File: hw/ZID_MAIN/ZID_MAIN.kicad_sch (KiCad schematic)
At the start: 201 parts, among them J1 Conn 1x04 0.1" Socket, J10 FFC/FPC-40 Socket, J11 JST-PH-K B6B, J12 JST-PH-K B6B, J13 Conn_02x05_PINHDR_2.54mm, J14 USB-C PWR ONLY, J2 JST-PH-K B6B, J3 Conn 1x02 0.1" pin, J4 Conn 1x03 0.1" pin, J5 Conn 1x08 0.1" pin, J6 Conn 1x08 0.1" pin, J7 Conn 2x04 0.1" pin, J8 Conn 2x02 0.1" pin, J9 Conn 2x04 0.1" pin, M1 WS-RP2040-Zero, SW1 SW_Push, SW2 SW_DIP_x02, U1 OSC-20MHz, U10 27WZ06, U11 74LVC125AS, U12 74LVC273, U13 74FCT2245, U14 AS7C1024B, U16 74FCT2245, U18 ATF1508AS, U2 74FCT2245, U20 74FCT2244, U22 ATF1504AS-44T, U23 74AHCT00, U24 74FCT2244, U25 ATF1504AS-44T, U26 ATF1504AS-44T, U27 ATF1504AS-44T, U28 ATF1504AS-44T, U3 24LC32, U4 MIC2775, U5 SST39SF010, U6 74LVC245, U7 74FCT2245, U8 74AHCT14, U9 Z80 C20MHz-PLCC

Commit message: SCHM: Updates per SM. PLD: comment corrections. PCB: start routing.
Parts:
- removed C12, C13, C14, C15, C16, C17, C18, C19, C35, C36, C37, C38: 0.1uF, Capacitor_SMD:C_0603_1608Metric, symbol Device:C_Small
- removed JC1, JD1: SolderJumper_2_Open, Jumper:SolderJumper-2_P1.3mm_Open_TrianglePad1.0x1.5mm, symbol Jumper:SolderJumper_2_Open
- removed JP5: Jumper_2_Small_Bridged, Connector_PinHeader_2.00mm:PinHeader_1x02_P2.00mm_Vertical, symbol Jumper:Jumper_2_Small_Bridged
- removed OP4: AES-Option_A-B_2mm, Connector_PinHeader_2.00mm:PinHeader_1x03_P2.00mm_Vertical, symbol AES_Library:AES-Option_A-B_2mm
- removed R43: 4.7k, Resistor_SMD:R_0805_2012Metric, symbol Device:R_Small_US
- removed SPRU8F1: Conn_01x03_Pin, Connector_PinHeader_2.00mm:PinHeader_1x03_P2.00mm_Vertical, symbol Connector:Conn_01x03_Pin
- removed TP12, TP26, TP28, TP29, TP31, TP32, TP33, TP34: TestPoint, TestPoint:TestPoint_THTPad_D1.0mm_Drill0.5mm, symbol Connector:TestPoint
- removed U25, U26, U27, U28: ATF1504AS-44T, Package_QFP:TQFP-44_10x10mm_P0.8mm, symbol AES_Library:ATF1504AS-44T-AES
- added DBOPT1: AES-Option_A-B_2mm, Connector_PinHeader_2.00mm:PinHeader_1x03_P2.00mm_Vertical, symbol AES_Library:AES-Option_A-B_2mm
- added J15: Conn 2x03 pin hdr 0.1", Connector_PinHeader_2.00mm:PinHeader_2x03_P2.00mm_Vertical, symbol Connector_Generic:Conn_02x03_Odd_Even
- added R34: 100k, Resistor_SMD:R_0805_2012Metric, symbol Device:R_Small_US
- added TP19, TP20, TP23, TP24: TestPoint, TestPoint:TestPoint_THTPad_D1.0mm_Drill0.5mm, symbol Connector:TestPoint
- added U15: ATF1508AS, Package_QFP:TQFP-100_14x14mm_P0.5mm, symbol AES_Library:ATF1508AS-AES
- R14: value 10k -> 100K; footprint Resistor_SMD:R_0805_2012Metric -> Resistor_SMD:R_0805_2012Metric_Pad1.20x1.40mm_HandSolder
- R23: value 10k -> 100k
- R42: value 4.7k -> 100k
- RN1, RN2: value 20k -> 100k
- TP17, TP18, TP21, TP22: Function IO8 -> IO1
- TP25: Function IO10 -> IO1
- U16: symbol AES_Library:74245_BA-AES -> AES_Library:74FCT2245-AES
- U22: Function BRK1&2n Addr Cmp -> BRK DATA, TGTGO & GPIO; ISP_CN ISP#2 -> ISP#3
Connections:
- net IOBD25 is gone; now on net SBC_IO: U22.10 (BMC25/IO)
- net IOBD51 is gone; now on net SBC_GPI3: U22.28 (DMC51/IO)
- net PU is gone; now on net +5V: R25.1, U14.30 (CS2/CE2)
- net +5V: now also R14.2, U20.11 (Ib3), U20.13 (Ib2), U20.15 (Ib1), R34.1, U15.18 (VCCIO), U15.3 (VCCIO), U15.34 (VCCIO), U15.39 (VCCINT), U15.51 (VCCIO), U15.66 (VCCIO), U15.82 (VCCIO), U15.91 (VCCINT); no longer R14.1, R25.2
- net BRD_RST-: now also DBOPT1.3 (B)
- net GND: now also R44.1, U15.11 (GND), U15.26 (GND), U15.38 (GND), U15.43 (GND), U15.59 (GND), U15.74 (GND), U15.86 (GND), U15.95 (GND); no longer R44.2
- net JTCK: now also U15.62 (F96/IO/JT.TCK)
- net JTD1O2I: now also J15.3 (Pin_3); no longer U22.1 (A8/IO/JT.TDI)
- net JTD2O3I: now also U22.1 (A8/IO/JT.TDI), U15.73 (G112/IO/JT.TDO); no longer U22.32 (D56/IO/JT.TDO)
- net JTDO_CI: now also J15.1 (Pin_1), J15.6 (Pin_6)
- net JTMS: now also U15.15 (C48/IO/JT.TMS)
- net PC_LATCH-: now also U15.87 (IN/GCK1)
- net SBC_GPI0: now also U16.14 (B4), U22.30 (DMC52/IO); no longer U16.6 (A4), U22.35 (D41/IO/GCK3)
- net SBC_GPI1: now also U16.13 (B5), U22.34 (DMC62/IO); no longer U16.7 (A5), U22.33 (DMC57/IO)
- net SBC_GPI2: now also U16.12 (B6), U22.27 (DMC49/IO); no longer U16.8 (A6), U22.30 (DMC52/IO)
- net SBC_GPI3: no longer U22.31 (DMC53/IO)
- net SBC_GPO0: now also U16.2 (A0), U22.44 (AMC11/IO); no longer U16.18 (B0), U22.43 (AMC14/IO)
- net SBC_GPO1: now also U16.3 (A1); no longer U16.17 (B1)
- net SBC_GPO2: now also U16.4 (A2), U22.43 (AMC14/IO); no longer U16.16 (B2), U22.44 (AMC11/IO)
- net SBC_GPO3: now also U16.5 (A3); no longer U16.15 (B3)
- net SBC_I0: now also R23.2, U16.6 (A4); no longer U16.14 (B4)
- net SBC_I1: now also U16.7 (A5), R34.2; no longer U16.13 (B5)
- net SBC_I2: now also R42.2, U16.8 (A6); no longer U16.12 (B6)
- net SBC_IO: no longer U22.18 (CMC33/IO)
- net SBC_O0: now also U16.18 (B0); no longer U16.2 (A0)
- net SBC_O1: now also U16.17 (B1); no longer U16.3 (A1)
- net SBC_O2: now also U16.16 (B2); no longer U16.4 (A2)
- net SBC_O3: now also U16.15 (B3); no longer U16.5 (A3)
- net TGTMODE-: now also U22.31 (DMC53/IO); no longer U22.27 (DMC49/IO)
- net TM1-: now also U16.11 (B7); no longer U16.9 (A7)
- net ZA0: now also U22.13 (BMC20/IO), U15.94 (AMC13/IO)
- net ZA1: now also U22.12 (BMC21/IO), U15.93 (AMC14/IO); no longer U22.15 (BMC17/IO)
- net ZA10: now also U15.40 (EMC65/IO)
- net ZA11: now also U15.41 (E67/IO/PD2)
- net ZA12: now also U15.42 (EMC69/IO)
- net ZA13: now also U15.44 (EMC70/IO)
- net ZA14: now also U15.45 (EMC72/IO)
- net ZA15: now also U15.46 (EMC73/IO)
- net ZA2: now also U22.15 (BMC17/IO), U15.6 (BMC29/IO); no longer U22.14 (BMC19/IO)
- net ZA3: now also U22.14 (BMC19/IO), U15.5 (BMC30/IO); no longer U22.13 (BMC20/IO)
- net ZA4: now also U15.48 (EMC77/IO); no longer U22.12 (BMC21/IO)
- net ZA5: now also U15.49 (EMC78/IO)
- net ZA6: now also U15.52 (FMC81/IO)
- net ZA7: now also U15.53 (FMC83/IO)
- net ZA8: now also U15.47 (EMC75/IO)
- net ZA9: now also U15.28 (DMC62/IO)
- net ZD0: now also U15.2 (AMC1/IO)
- net ZD1: now also U15.100 (AMC5/IO)
- net ZD2: now also U22.25 (CMC46/IO), U15.1 (A3/IO/PD1); no longer U22.22 (CMC40/IO)
- net ZD3: now also U22.22 (CMC40/IO), U15.99 (AMC6/IO); no longer U22.25 (CMC46/IO)
- net ZD4: now also U22.6 (AMC1/IO), U15.97 (AMC9/IO); no longer U22.23 (CMC41/IO)
- net ZD5: now also U22.23 (CMC41/IO), U15.98 (AMC8/IO); no longer U22.6 (AMC1/IO)
- net ZD6: now also U15.96 (AMC11/IO)
- net ZD7: now also U15.92 (AMC16/IO)
- net ZM1-: now also U16.9 (A7); no longer U16.11 (B7)
- net ZRD-: now also U15.17 (CMC45/IO)
- net ZRST-: now also DBOPT1.1 (A)
- net ZWR-: now also U15.14 (BMC17/IO)
- net at U8.13: now also R14.1, TP3.1
- net at U8.12: now also TP7.1
- net at U9.30 (~{RESET}): now also DBOPT1.2 (C); no longer R14.2
- net VBUSP: now reaches J14.A4_B9 (VBUS), J14.B4_A9 (VBUS), JP7.1 (A)
- net at J14.SH1 (SHIELD), J14.SH2 (SHIELD), J14.SH3 (SHIELD)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: now also R44.2; no longer R44.1
- net ADDR_DOD: no longer names the net of TP18.1
- net ADDR_DOD: now also U15.79 (HMC120/IO)
- net AEN_CLK: no longer names the net of U18.57 (FMC89/IO)
- net AEN_CLK: now also TP10.1
- net AEN_CLR-: no longer names the net of U18.56 (FMC88/IO)
- net AEN_CLR-: now also TP11.1
- net BA_CLK: no longer names the net of U18.55 (FMC86/IO)
- net BA_CLR-: no longer names the net of U18.58 (FMC91/IO)
- net BRK1_AEQ- renamed BRK1_AEQ
- net BRK1_AEQ: now also U15.8 (BMC25/IO)
- net BRKHWDET-: no longer names the net of U18.76 (HMC115/IO)
- net BRKHWDET-: no longer R42.2
- net BRKN_AEQ- renamed BRKN_AEQ
- net BRKN_AEQ: now also U15.7 (BMC27/IO)
- net BRKPC_RD-: no longer names the net of U18.60 (FMC93/IO)
- net ENBL_DOD: no longer names the net of TP17.1
- net ENBL_DOD: now also U15.10 (BMC22/IO)
- net IO10C: no longer names the net of TP25.1
- net IO10C: now also U15.50 (EMC80/IO)
- net IO123: no longer names the net of U18.81 (HMC123/IO)
- net IO123: no longer TP3.1
- net IO62: no longer names the net of U18.28 (DMC62/IO)
- net IO62: no longer TP7.1
- net IO64: no longer names the net of TP6.1
- net IO64: now also U15.85 (H128/IO/GCK3); no longer U18.27 (DMC64/IO)
- net IO81: no longer names the net of U18.52 (FMC81/IO)
- net IO83: no longer names the net of U18.53 (FMC83/IO)
- net IO83: no longer TP11.1
- net IO85: no longer names the net of U18.54 (FMC85/IO)
- net IO85: no longer TP10.1
- net IO8C: no longer names the net of TP21.1
- net IO8C: now also U15.70 (GMC107/IO)
- net IO8D: no longer names the net of TP22.1
- net IO8D: now also U22.18 (CMC33/IO)
- net IOBD24: no longer names the net of TP13.1
- net IOBD24: now also U22.35 (D41/IO/GCK3); no longer U22.11 (BMC24/IO)
- net MEM_OP- renamed MEM_OP
- net PCRD_DIN: no longer names the net of U18.77 (HMC117/IO)
- net TGT_GO: no longer names the net of U18.61 (FMC94/IO)
- net TGT_GO: no longer U22.34 (DMC62/IO)
- new net: TP19.1, U15.20 (CMC41/IO)
- new net: TP23.1, U15.31 (DMC57/IO)
- new net: TP24.1, U15.56 (FMC88/IO)
- new net: TP20.1, U22.33 (DMC57/IO)
- new net D2_IN: J15.5 (Pin_5), R25.2, U15.4 (B32/IO/JT.TDI)
- new net JTD3OCI: J15.4 (Pin_4), U22.32 (D56/IO/JT.TDO)
- new net ZID_IO: U15.68 (GMC104/IO), U18.27 (DMC64/IO), U22.11 (BMC24/IO)
- no-connect marks 18 -> 72
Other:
- moved on the sheet: C1, C2, C20, C21, C22, C23, C24, C25, C26, C27, C28, C29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

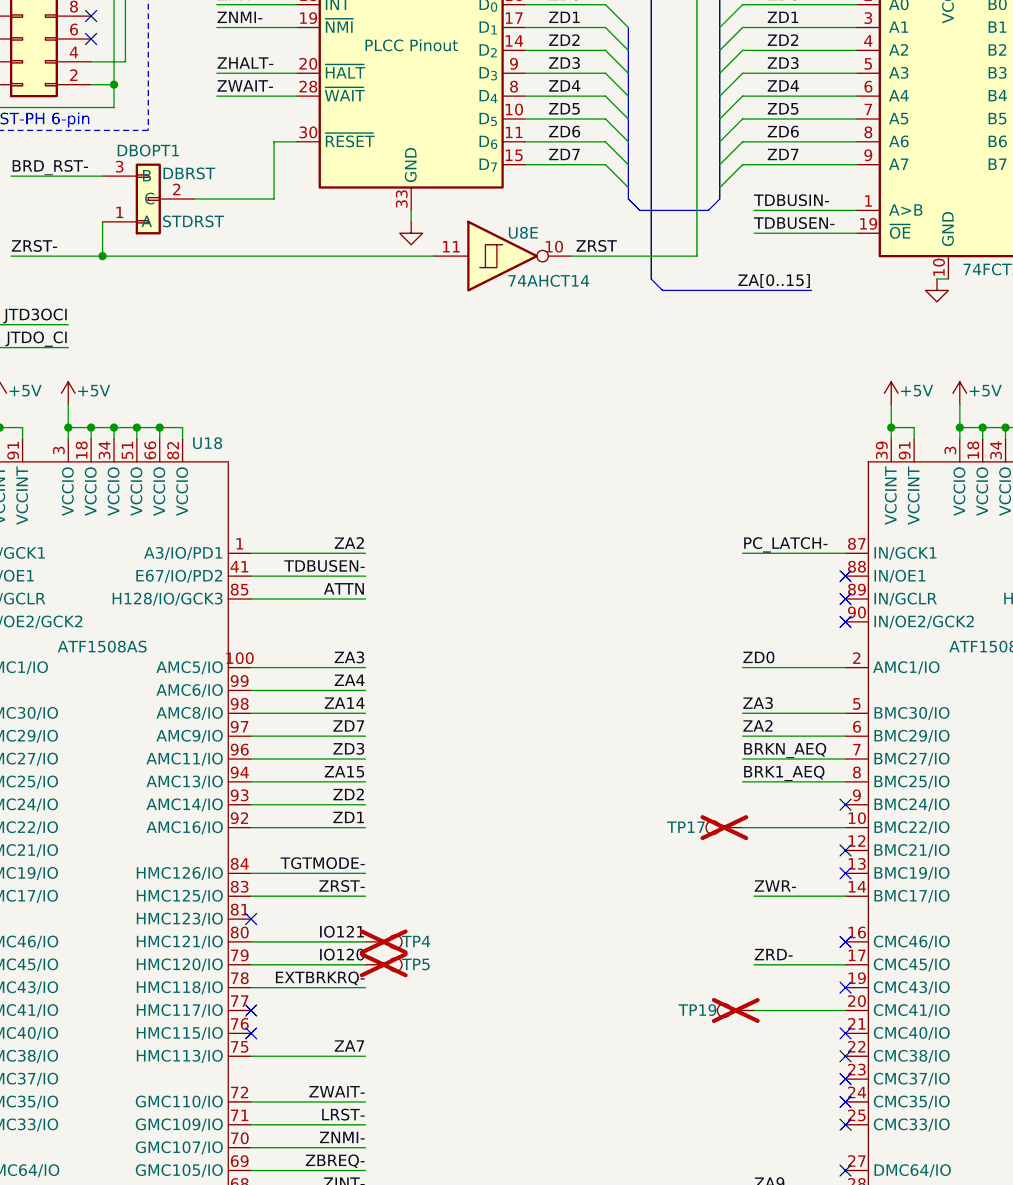
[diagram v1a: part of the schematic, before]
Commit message: SCHM/PCB: Small pin assignment changes on U15.
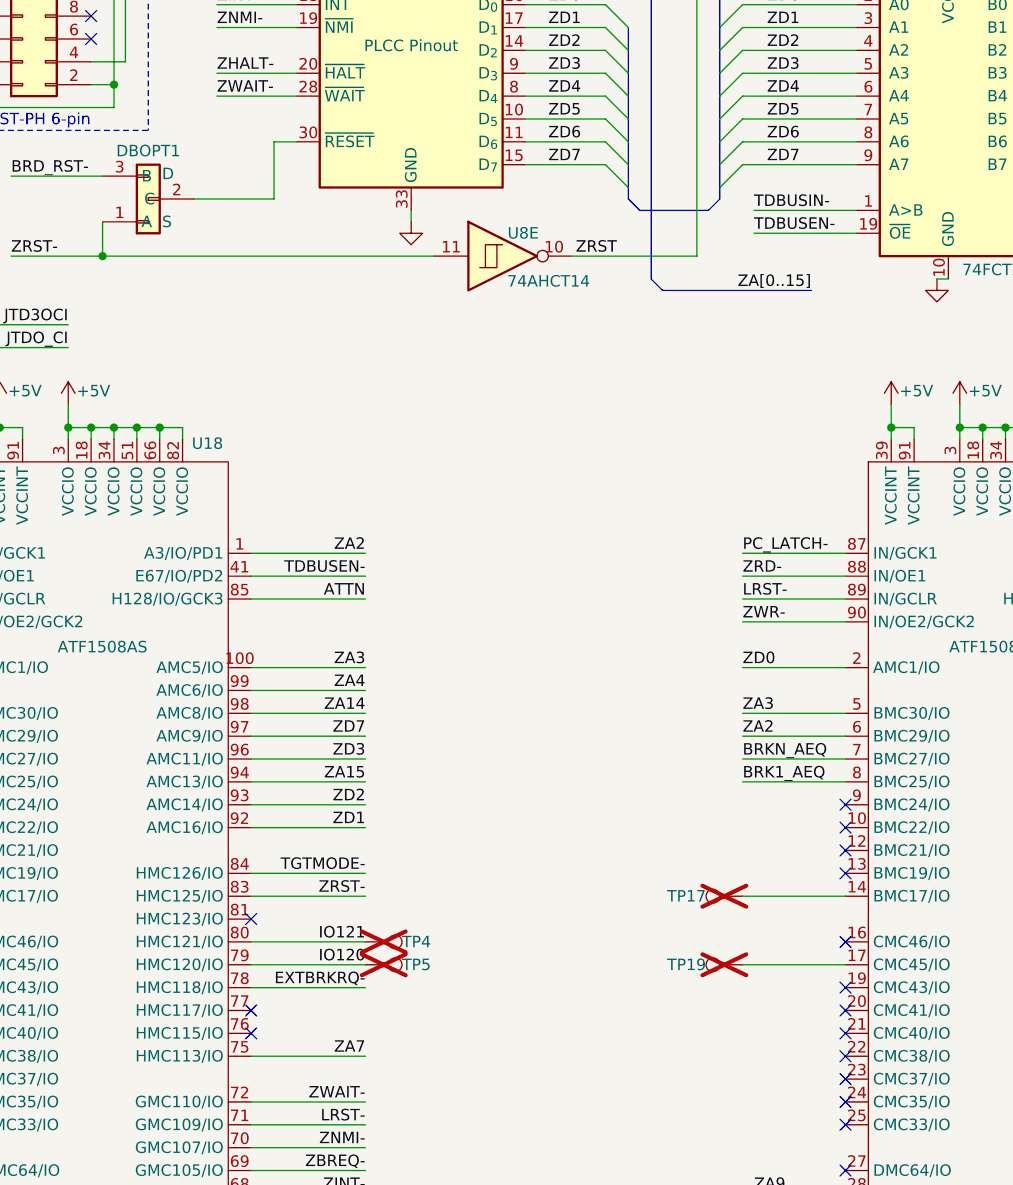
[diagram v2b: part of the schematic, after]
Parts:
- DBOPT1: OP1-2 STDRST -> S; OP2-3 DBRST -> D
- J5: P1 (none) -> GND; P2 (none) -> ZRFSH; P2B (none) -> ZRFSH; P3 (none) -> ZM1; P4 (none) -> ZMREQ; P5 (none) -> ZIORQ; P6 (none) -> ZRD; P7 (none) -> ZWR; P8 (none) -> ZWAIT
- J6: P1B (none) -> D0; P2 (none) -> D1; P3 (none) -> D2; P4 (none) -> D3; P5 (none) -> D4; P6 (none) -> D5; P7 (none) -> D6; P8 (none) -> D7
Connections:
- net LRST-: now also U15.89 (IN/GCLR)
- net ZRD-: now also U15.88 (IN/OE1); no longer U15.17 (CMC45/IO)
- net ZWR-: now also U15.90 (IN/OE2/GCK2); no longer U15.14 (BMC17/IO)
- net at U15.10 (BMC22/IO): no longer TP17.1
- net at TP19.1: now also U15.17 (CMC45/IO); no longer U15.20 (CMC41/IO)
- new net: TP17.1, U15.14 (BMC17/IO)
- no-connect marks 72 -> 71
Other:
- moved on the sheet: TP17, TP19
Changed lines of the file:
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@@
 	)
 	(no_connect
-		(at 133.35 163.83)
-	)
-	(no_connect
 		(at 133.35 234.95)
 	)
@@
 	)
 	(no_connect
+		(at 133.35 191.77)
+	)
+	(no_connect
 		(at 166.37 260.35)
 	)
@@
 	)
 	(no_connect
-		(at 133.35 168.91)
-	)
-	(no_connect
 		(at 133.35 189.23)
 	)
@@
 	)
 	(no_connect
+		(at 133.35 212.09)
+	)
+	(no_connect
 		(at 49.53 104.14)
 	)
@@
 	)
 	(no_connect
-		(at 133.35 166.37)
-	)
-	(no_connect
 		(at 233.68 313.69)
 	)
@@
 	(wire
 		(pts
+			(xy 121.92 166.37) (xy 133.35 166.37)
+		)
+		(stroke
+			(width 0)
+			(type default)
+		)
+	)
+	(wire
+		(pts
 			(xy 321.31 99.06) (xy 327.66 99.06)
 		)
@@
 	(wire
 		(pts
+			(xy 121.92 163.83) (xy 133.35 163.83)
+		)
+		(stroke
+			(width 0)
+			(type default)
+		)
+	)
+	(wire
+		(pts
 			(xy 29.21 322.58) (xy 29.21 330.2)
 		)
@@
 	(wire
 		(pts
-			(xy 123.19 199.39) (xy 133.35 199.39)
+			(xy 121.92 199.39) (xy 133.35 199.39)
 		)
 		(stroke
@@
 	(wire
 		(pts
+			(xy 121.92 168.91) (xy 133.35 168.91)
+		)
+		(stroke
+			(width 0)
+			(type default)
+		)
+	)
+	(wire
+		(pts
 			(xy 158.75 312.42) (xy 158.75 317.5)
 		)
@@
 	(wire
 		(pts
-			(xy 123.19 207.01) (xy 133.35 207.01)
+			(xy 121.92 207.01) (xy 133.35 207.01)
 		)
 		(stroke
@@
 		)
 	)
-	(wire
-		(pts
-			(xy 123.19 212.09) (xy 133.35 212.09)
-		)
-		(stroke
-			(width 0)
-			(type default)
-		)
-	)
 	(bus
 		(pts
@@
 	(wire
 		(pts
-			(xy 121.92 191.77) (xy 133.35 191.77)
-		)
-		(stroke
-			(width 0)
-			(type default)
-		)
-	)
-	(wire
-		(pts
 			(xy 44.45 312.42) (xy 39.37 312.42)
 		)
@@
 		)
 	)
+	(label "ZWR-"
+		(at 121.92 168.91 0)
+		(effects
+			(font
+				(size 1.27 1.27)
+			)
+			(justify left bottom)
+		)
+	)
 	(label "BRD_RST-"
 		(at 40.64 119.38 0)
@@
 		)
 	)
+	(label "ZRD-"
+		(at 121.92 163.83 0)
+		(effects
+			(font
+				(size 1.27 1.27)
+			)
+			(justify left bottom)
+		)
+	)
 	(label "ZA4"
 		(at 200.66 111.76 180)
@@
 		)
 	)
-	(label "ZRD-"
-		(at 123.19 207.01 0)
-		(effects
-			(font
-				(size 1.27 1.27)
-			)
-			(justify left bottom)
-		)
-	)
 	(label "V3D6"
 		(at 312.42 72.39 0)
@@
 		)
 	)
+	(label "LRST-"
+		(at 121.92 166.37 0)
+		(effects
+			(font
+				(size 1.27 1.27)
+			)
+			(justify left bottom)
+		)
+	)
 	(label "ZA8"
 		(at 200.66 121.92 180)
@@
 		)
 	)
-	(label "ZWR-"
-		(at 123.19 199.39 0)
-		(effects
-			(font
-				(size 1.27 1.27)
-			)
-			(justify left bottom)
-		)
-	)
 	(label "ZA6"
 		(at 132.08 21.59 180)
@@
 			)
 		)
+		(property "P2" "ZRFSH"
+			(at 101.6 35.56 0)
+			(effects
+				(font
+					(size 1.27 1.27)
+				)
+				(hide yes)
+			)
+		)
+		(property "P3" "ZM1"
+			(at 101.6 35.56 0)
+			(effects
+				(font
+					(size 1.27 1.27)
+				)
+				(hide yes)
+			)
+		)
+		(property "P4" "ZMREQ"
+			(at 101.6 35.56 0)
+			(effects
+				(font
+					(size 1.27 1.27)
+				)
+				(hide yes)
+			)
+		)
+		(property "P5" "ZIORQ"
+			(at 101.6 35.56 0)
+			(effects
+				(font
+					(size 1.27 1.27)
+				)
+				(hide yes)
+			)
+		)
+		(property "P6" "ZRD"
+			(at 101.6 35.56 0)
+			(effects
+				(font
+					(size 1.27 1.27)
+				)
+				(hide yes)
+			)
+		)
+		(property "P7" "ZWR"
+			(at 101.6 35.56 0)
+			(effects
+				(font
+					(size 1.27 1.27)
+				)
+				(hide yes)
+			)
+		)
+		(property "P8" "ZWAIT"
+			(at 101.6 35.56 0)
+			(effects
+				(font
+					(size 1.27 1.27)
+				)
+				(hide yes)
+			)
+		)
+		(property "P1" "GND"
+			(at 101.6 35.56 0)
+			(effects
+				(font
+					(size 1.27 1.27)
+				)
+				(hide yes)
+			)
+		)
+		(property "P2B" "ZRFSH"
+			(at 101.6 35.56 0)
+			(effects
+				(font
+					(size 1.27 1.27)
+				)
+				(hide yes)
+			)
+		)
 		(pin "3"
 		)
@@
 	(symbol
 		(lib_id "Connector:TestPoint")
-		(at 123.19 212.09 90)
+		(at 121.92 207.01 90)
 		(unit 1)
 		(exclude_from_sim no)
@@
 		(dnp yes)
 		(property "Reference" "TP19"
-			(at 119.126 212.09 90)
+			(at 117.856 207.01 90)
 			(effects
 				(font
@@
 		)
 		(property "Value" "TestPoint"
-			(at 119.888 209.55 90)
+			(at 118.618 204.47 90)
 			(effects
 				(font
@@
 		)
 		(property "Footprint" "TestPoint:TestPoint_THTPad_D1.0mm_Drill0.5mm"
-			(at 123.19 207.01 0)
+			(at 121.92 201.93 0)
 			(effects
 				(font
@@
 		)
 		(property "Datasheet" "~"
-			(at 123.19 207.01 0)
+			(at 121.92 201.93 0)
 			(effects
 				(font
@@
 		)
 		(property "Description" "test point"
-			(at 123.19 212.09 0)
+			(at 121.92 207.01 0)
 			(effects
 				(font
@@
 		)
 		(property "Function" "IO1"
-			(at 123.19 212.09 90)
+			(at 121.92 207.01 90)
 			(effects
 				(font
@@
 			)
 		)
+		(property "P1B" "D0"
+			(at 179.07 107.95 0)
+			(effects
+				(font
+					(size 1.27 1.27)
+				)
+				(hide yes)
+			)
+		)
+		(property "P2" "D1"
+			(at 179.07 107.95 0)
+			(effects
+				(font
+					(size 1.27 1.27)
+				)
+				(hide yes)
+			)
+		)
+		(property "P3" "D2"
+			(at 179.07 107.95 0)
+			(effects
+				(font
+					(size 1.27 1.27)
+				)
+				(hide yes)
+			)
+		)
+		(property "P4" "D3"
+			(at 179.07 107.95 0)
+			(effects
+				(font
+					(size 1.27 1.27)
+				)
+				(hide yes)
+			)
+		)
+		(property "P5" "D4"
+			(at 179.07 107.95 0)
+			(effects
+				(font
+					(size 1.27 1.27)
+				)
+				(hide yes)
+			)
+		)
+		(property "P6" "D5"
+			(at 179.07 107.95 0)
+			(effects
+				(font
+					(size 1.27 1.27)
+				)
+				(hide yes)
+			)
+		)
+		(property "P7" "D6"
+			(at 179.07 107.95 0)
+			(effects
+				(font
+					(size 1.27 1.27)
+				)
+				(hide yes)
+			)
+		)
+		(property "P8" "D7"
+			(at 179.07 107.95 0)
+			(effects
+				(font
+					(size 1.27 1.27)
+				)
+				(hide yes)
+			)
+		)
 		(pin "3"
 		)
@@
 			)
 		)
-		(property "OP1-2" "STDRST"
+		(property "OP1-2" "S"
 			(at 57.404 124.46 0)
 			(effects
@@
 			)
 		)
-		(property "OP2-3" "DBRST"
+		(property "OP2-3" "D"
 			(at 57.404 119.126 0)
 			(effects
@@
 	(symbol
 		(lib_id "Connector:TestPoint")
-		(at 121.92 191.77 90)
+		(at 121.92 199.39 90)
 		(unit 1)
 		(exclude_from_sim no)
@@
 		(dnp yes)
 		(property "Reference" "TP17"
-			(at 117.856 191.77 90)
+			(at 117.856 199.39 90)
 			(effects
 				(font
@@
 		)
 		(property "Value" "TestPoint"
-			(at 118.618 189.23 90)
+			(at 118.618 196.85 90)
 			(effects
 				(font
@@
 		)
 		(property "Footprint" "TestPoint:TestPoint_THTPad_D1.0mm_Drill0.5mm"
-			(at 121.92 186.69 0)
+			(at 121.92 194.31 0)
 			(effects
 				(font
@@
 		)
 		(property "Datasheet" "~"
-			(at 121.92 186.69 0)
+			(at 121.92 194.31 0)
 			(effects
 				(font
@@
 		)
 		(property "Description" "test point"
-			(at 121.92 191.77 0)
+			(at 121.92 199.39 0)
 			(effects
 				(font
@@
 		)
 		(property "Function" "IO1"
-			(at 121.92 191.77 90)
+			(at 121.92 199.39 90)
 			(effects
 				(font

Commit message: PCB: AB+PCL pinout. Exp-BP add position.
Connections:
- net BRK1_AEQ: now also U15.93 (AMC14/IO); no longer U15.8 (BMC25/IO)
- net BRKN_AEQ: now also U15.92 (AMC16/IO); no longer U15.7 (BMC27/IO)
- net ZA0: now also U15.96 (AMC11/IO); no longer U15.94 (AMC13/IO)
- net ZA1: now also U15.7 (BMC27/IO); no longer U15.93 (AMC14/IO)
- net ZA10: now also U15.57 (FMC89/IO); no longer U15.40 (EMC65/IO)
- net ZA11: now also U15.98 (AMC8/IO); no longer U15.41 (E67/IO/PD2)
- net ZA12: now also U15.47 (EMC75/IO); no longer U15.42 (EMC69/IO)
- net ZA13: now also U15.13 (BMC19/IO); no longer U15.44 (EMC70/IO)
- net ZA14: now also U15.49 (EMC78/IO); no longer U15.45 (EMC72/IO)
- net ZA3: now also U15.9 (BMC24/IO); no longer U15.5 (BMC30/IO)
- net ZA4: now also U15.100 (AMC5/IO); no longer U15.48 (EMC77/IO)
- net ZA5: now also U15.1 (A3/IO/PD1); no longer U15.49 (EMC78/IO)
- net ZA6: now also U15.2 (AMC1/IO); no longer U15.52 (FMC81/IO)
- net ZA7: now also U15.99 (AMC6/IO); no longer U15.53 (FMC83/IO)
- net ZA8: now also U15.60 (FMC93/IO); no longer U15.47 (EMC75/IO)
- net ZA9: now also U15.10 (BMC22/IO); no longer U15.28 (DMC62/IO)
- net ZD0: now also U15.24 (CMC35/IO); no longer U15.2 (AMC1/IO)
- net ZD1: now also U15.23 (CMC37/IO); no longer U15.100 (AMC5/IO)
- net ZD2: now also U15.22 (CMC38/IO); no longer U15.1 (A3/IO/PD1)
- net ZD3: now also U15.21 (CMC40/IO); no longer U15.99 (AMC6/IO)
- net ZD4: now also U15.20 (CMC41/IO); no longer U15.97 (AMC9/IO)
- net ZD5: now also U15.19 (CMC43/IO); no longer U15.98 (AMC8/IO)
- net ZD6: now also U15.17 (CMC45/IO); no longer U15.96 (AMC11/IO)
- net ZD7: now also U15.16 (CMC46/IO); no longer U15.92 (AMC16/IO)
- net ZID_IO: now also U15.28 (DMC62/IO); no longer U15.68 (GMC104/IO)
- net at TP6.1: now also U15.97 (AMC9/IO); no longer U15.85 (H128/IO/GCK3)
- net at TP25.1: now also U15.45 (EMC72/IO); no longer U15.50 (EMC80/IO)
- net at U15.14 (BMC17/IO): no longer TP17.1
- net at TP19.1: now also U15.25 (CMC33/IO); no longer U15.17 (CMC45/IO)
- net at U15.31 (DMC57/IO): no longer TP23.1
- net at U15.33 (DMC54/IO): now also TP23.1
- net at TP21.1: now also U15.68 (GMC104/IO); no longer U15.70 (GMC107/IO)
- new net: TP17.1, U15.5 (BMC30/IO)
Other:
- moved on the sheet: TP17, TP18, TP19, TP21, TP23, TP25, TP6

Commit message: PCB layout progress before SRAM move. PLD: Allow upper-8 address only on BRK1.
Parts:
- added TP12: TestPoint, TestPoint:TestPoint_THTPad_D1.0mm_Drill0.5mm, symbol Connector:TestPoint
- added U17, U19: 74HCT166, Package_SO:SOIC-16_3.9x9.9mm_P1.27mm, symbol AES_Library:74166-AES
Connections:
- net +5V: now also U17.16 (VCC), U17.9 (~{Clr}), U19.16 (VCC), U19.9 (~{Clr})
- net GND: now also U17.1 (Ds), U17.6 (~{CE}), U17.8 (GND), U19.6 (~{CE}), U19.8 (GND)
- net PC_LATCH-: now also U17.7 (Clk), U19.7 (Clk)
- net TGTMODE-: now also TP12.1, U17.15 (~{LD}), U19.15 (~{LD})
- net ZA0: now also U19.14 (H)
- net ZA1: now also U19.12 (G)
- net ZA10: now also U17.11 (F)
- net ZA11: now also U17.10 (E)
- net ZA12: now also U17.5 (D)
- net ZA13: now also U17.4 (C)
- net ZA14: now also U17.3 (B)
- net ZA15: now also U17.2 (A)
- net ZA2: now also U19.11 (F)
- net ZA3: now also U19.10 (E)
- net ZA4: now also U19.5 (D)
- net ZA5: now also U19.4 (C)
- net ZA6: now also U19.3 (B)
- net ZA7: now also U19.2 (A)
- net ZA8: now also U17.14 (H)
- net ZA9: now also U17.12 (G)
- net at U15.25 (CMC33/IO): now also TP23.1; no longer TP19.1
- net at U15.33 (DMC54/IO): now also TP19.1; no longer TP23.1
- net IO59 renamed PCRD_DIN
- net PCRD_DIN: now also U19.13 (Qh)
- new net: U17.13 (Qh), U19.1 (Ds)
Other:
- title: Z80 In-Circuit Debugger (ZID) -> Z80 In-Circuit Debugger (ZID) and SBC
- moved on the sheet: C1, C10, C11, C2, C20, C21, C22, C23, C24, C25, C26, C27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
